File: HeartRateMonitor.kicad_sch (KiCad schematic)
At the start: 18 parts, among them J1 USB_C_Receptacle_USB2.0, U1 CH340E, U2 STM32G071KxT

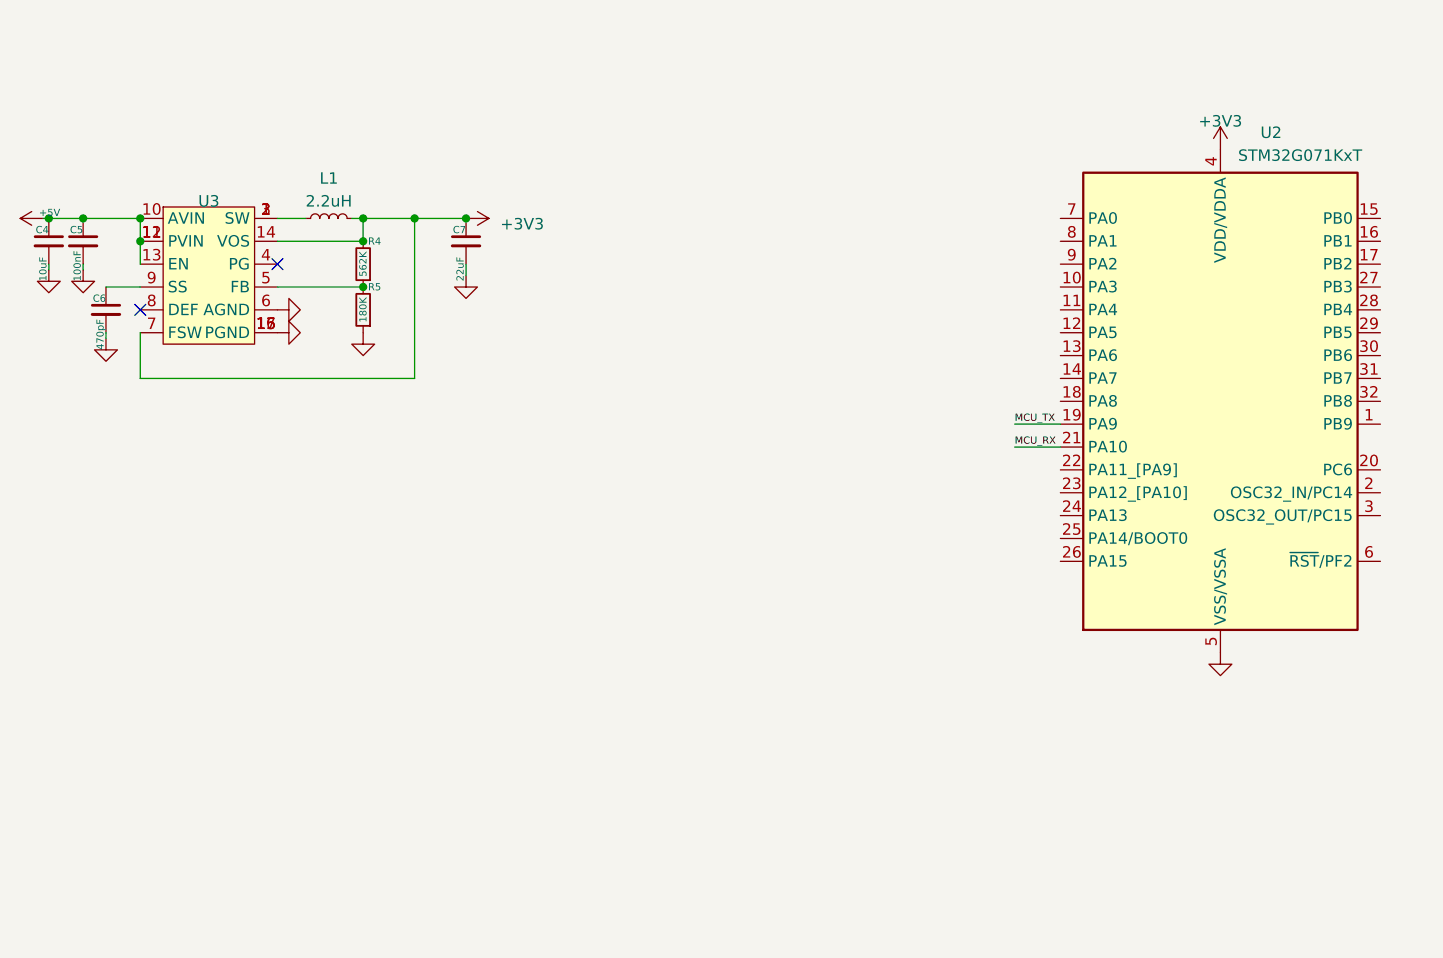
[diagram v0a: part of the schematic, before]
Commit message: firmware template and PCB constrains
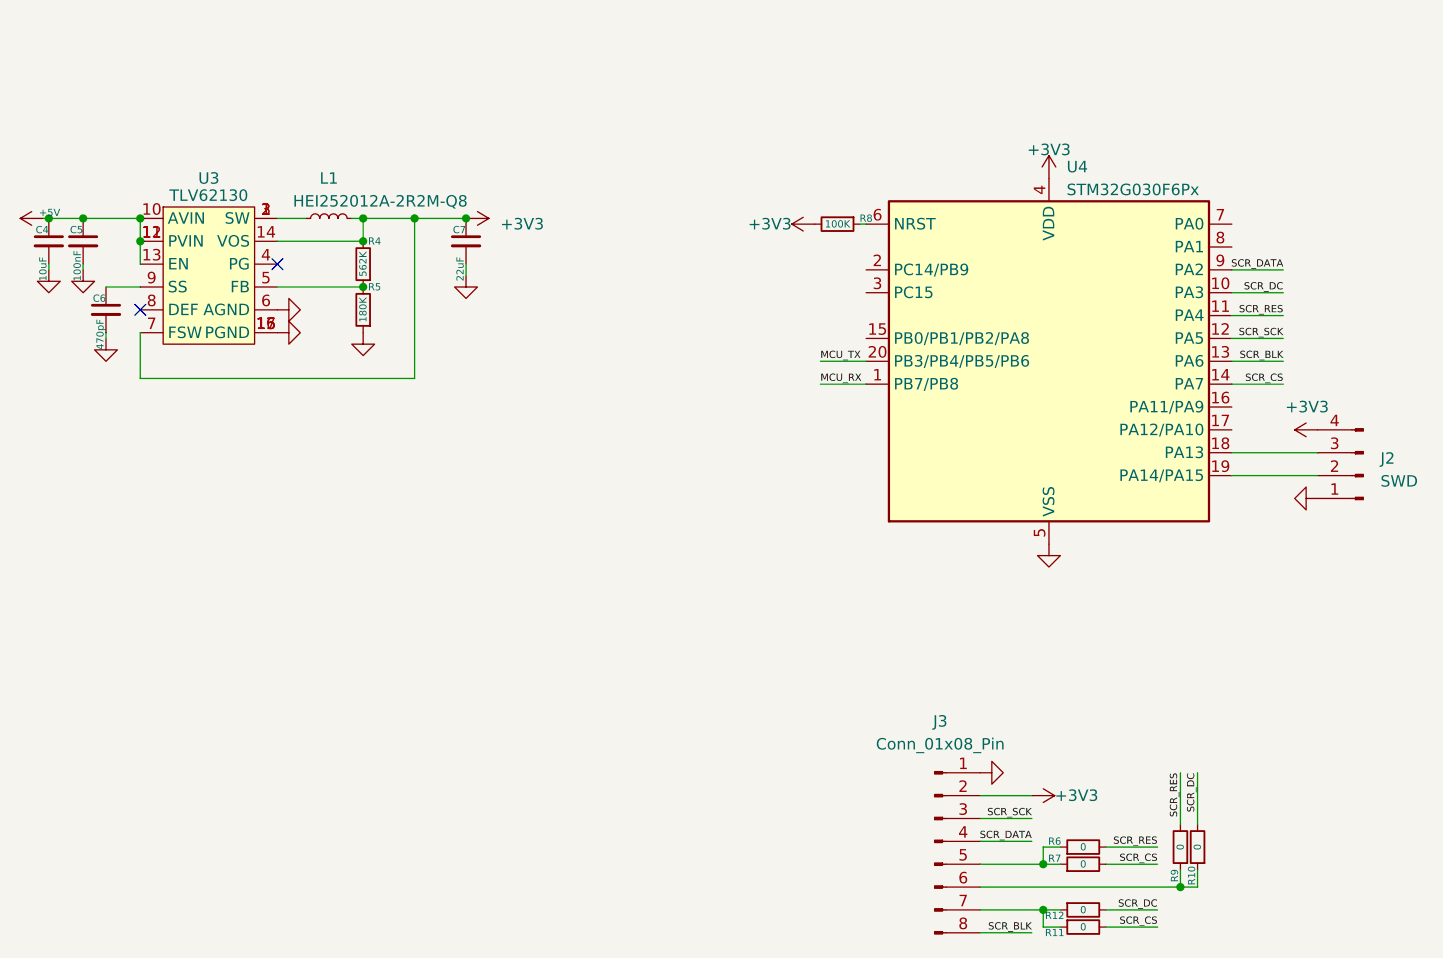
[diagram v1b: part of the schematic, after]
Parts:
- removed U2: STM32G071KxT, Package_QFP:LQFP-32_7x7mm_P0.8mm, symbol MCU_ST_STM32G0:STM32G071KxT
- added J2: SWD, Connector_PinHeader_2.54mm:PinHeader_1x04_P2.54mm_Vertical, symbol Connector:Conn_01x04_Pin
- added J3: Conn_01x08_Pin, Connector_PinHeader_2.54mm:PinHeader_1x08_P2.54mm_Vertical, symbol Connector:Conn_01x08_Pin
- added R10, R11, R12, R6, R7, R9: 0, Resistor_SMD:R_0603_1608Metric, symbol Device:R_Small
- added R8: 100K, Resistor_SMD:R_0603_1608Metric, symbol Device:R_Small
- added U4: STM32G030F6Px, Package_SO:TSSOP-20_4.4x6.5mm_P0.65mm, symbol MCU_ST_STM32G0:STM32G030F6Px
- C1, C2, C3, C4, C5, C6, C7: footprint (none) -> Capacitor_SMD:C_0603_1608Metric
- F1: footprint (none) -> Fuse:Fuse_0805_2012Metric
- J1: footprint (none) -> FP:TYPE-C-31-M-31
- L1: value 2.2uH -> HEI252012A-2R2M-Q8; footprint (none) -> Inductor_SMD:L_1008_2520Metric
- R1, R2, R3, R4, R5: footprint (none) -> Resistor_SMD:R_0603_1608Metric
- U3: value ~ -> TLV62130; footprint (none) -> Package_DFN_QFN:VQFN-16-1EP_3x3mm_P0.5mm_EP1.68x1.68mm
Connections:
- net +3V3: now also J2.4 (Pin_4), J3.2 (Pin_2), R8.2, U4.4 (VDD)
- net GND: now also J2.1 (Pin_1), J3.1 (Pin_1), U4.5 (VSS)
- net MCU_RX: now also U4.1 (PB7/PB8)
- net MCU_TX: now also U4.20 (PB3/PB4/PB5/PB6)
- new net: J3.7 (Pin_7), R11.1, R12.1
- new net: J3.5 (Pin_5), R6.1, R7.1
- new net: J2.2 (Pin_2), U4.19 (PA14/PA15)
- new net: J2.3 (Pin_3), U4.18 (PA13)
- new net: R8.1, U4.6 (NRST)
- new net: J3.6 (Pin_6), R10.1, R9.1
- new net SCR_BLK: J3.8 (Pin_8), U4.13 (PA6)
- new net SCR_CS: R11.2, R7.2, U4.14 (PA7)
- new net SCR_DATA: J3.4 (Pin_4), U4.9 (PA2)
- new net SCR_DC: R10.2, R12.2, U4.10 (PA3)
- new net SCR_RES: R6.2, R9.2, U4.11 (PA4)
- new net SCR_SCK: J3.3 (Pin_3), U4.12 (PA5)

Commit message: add TIA
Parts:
- added C8: 150pF, Capacitor_SMD:C_0603_1608Metric, symbol Device:C_Small
- added R13: 500K, Resistor_SMD:R_0603_1608Metric, symbol Device:R_Small
- added U2: LMH6702MF, Package_TO_SOT_SMD:SOT-23-5, symbol Amplifier_Operational:LMH6702MF
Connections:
- net +3V3: now also U2.5 (V+)
- net GND: now also U2.3 (+)
- new net: C8.1, R13.1, U2.4 (-)
- new net: C8.2, R13.2, U2.1
- new net -3V3: U2.2 (V-)
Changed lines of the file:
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@@
   (junction (at 139.7 37.465) (diameter 0) (color 0 0 0 0)
   )
+  (junction (at 72.39 99.06) (diameter 0) (color 0 0 0 0)
+  )
   (junction (at 114.935 40.005) (diameter 0) (color 0 0 0 0)
   )
   (junction (at 215.265 109.22) (diameter 0) (color 0 0 0 0)
   )
+  (junction (at 87.63 96.52) (diameter 0) (color 0 0 0 0)
+  )
+  (junction (at 72.39 110.49) (diameter 0) (color 0 0 0 0)
+  )
   (junction (at 51.435 31.115) (diameter 0) (color 0 0 0 0)
   )
@@
   )
   (junction (at 230.505 111.76) (diameter 0) (color 0 0 0 0)
+  )
+  (junction (at 66.04 99.06) (diameter 0) (color 0 0 0 0)
   )
   (junction (at 114.935 37.465) (diameter 0) (color 0 0 0 0)
@@
     (stroke (width 0) (type default))
   )
+  (wire (pts (xy 72.39 99.06) (xy 72.39 102.87))
+    (stroke (width 0) (type default))
+  )
   (wire (pts (xy 114.935 55.245) (xy 145.415 55.245))
     (stroke (width 0) (type default))
@@
     (stroke (width 0) (type default))
   )
+  (wire (pts (xy 72.39 110.49) (xy 66.04 110.49))
+    (stroke (width 0) (type default))
+  )
   (wire (pts (xy 145.415 55.245) (xy 145.415 37.465))
     (stroke (width 0) (type default))
@@
     (stroke (width 0) (type default))
   )
+  (wire (pts (xy 67.31 99.06) (xy 66.04 99.06))
+    (stroke (width 0) (type default))
+  )
   (wire (pts (xy 21.59 62.865) (xy 23.495 62.865))
     (stroke (width 0) (type default))
@@
     (stroke (width 0) (type default))
   )
+  (wire (pts (xy 87.63 96.52) (xy 92.71 96.52))
+    (stroke (width 0) (type default))
+  )
   (wire (pts (xy 208.28 111.76) (xy 230.505 111.76))
     (stroke (width 0) (type default))
@@
     (stroke (width 0) (type default))
   )
+  (wire (pts (xy 72.39 87.63) (xy 72.39 93.98))
+    (stroke (width 0) (type default))
+  )
+  (wire (pts (xy 72.39 107.95) (xy 72.39 110.49))
+    (stroke (width 0) (type default))
+  )
   (wire (pts (xy 67.31 55.245) (xy 67.31 56.515))
     (stroke (width 0) (type default))
@@
     (stroke (width 0) (type default))
   )
+  (wire (pts (xy 87.63 96.52) (xy 87.63 110.49))
+    (stroke (width 0) (type default))
+  )
   (wire (pts (xy 23.495 67.945) (xy 25.4 67.945))
     (stroke (width 0) (type default))
   )
+  (wire (pts (xy 87.63 110.49) (xy 72.39 110.49))
+    (stroke (width 0) (type default))
+  )
   (wire (pts (xy 139.7 37.465) (xy 138.43 37.465))
     (stroke (width 0) (type default))
@@
     (stroke (width 0) (type default))
   )
+  (wire (pts (xy 66.04 99.06) (xy 66.04 110.49))
+    (stroke (width 0) (type default))
+  )
   (wire (pts (xy 108.585 37.465) (xy 114.935 37.465))
     (stroke (width 0) (type default))
@@
   )
   (wire (pts (xy 51.435 29.845) (xy 51.435 31.115))
+    (stroke (width 0) (type default))
+  )
+  (wire (pts (xy 58.42 99.06) (xy 66.04 99.06))
     (stroke (width 0) (type default))
   )
@@
     )
   )
+  (symbol (lib_id "power:+3V3") (at 77.47 88.9 0) (unit 1)
+    (in_bom yes) (on_board yes) (dnp no) (fields_autoplaced)
+    (property "Reference" "#PWR025" (at 77.47 92.71 0)
+      (effects (font (size 1.27 1.27)) hide)
+    )
+    (property "Value" "+3V3" (at 77.47 85.09 0)
+      (effects (font (size 1.27 1.27)))
+    )
+    (property "Footprint" "" (at 77.47 88.9 0)
+      (effects (font (size 1.27 1.27)) hide)
+    )
+    (property "Datasheet" "" (at 77.47 88.9 0)
+      (effects (font (size 1.27 1.27)) hide)
+    )
+    (pin "1")
+    (instances
+      (project "HeartRateMonitor"
+        (path "/3e6a4c48-106f-4ca3-959b-b6cbb3b5c31c"
+          (reference "#PWR025") (unit 1)
+        )
+      )
+    )
+  )
   (symbol (lib_id "Device:L_Small") (at 135.89 37.465 90) (unit 1)
     (in_bom yes) (on_board yes) (dnp no)
@@
     )
   )
+  (symbol (lib_id "power:-3V3") (at 77.47 104.14 180) (unit 1)
+    (in_bom yes) (on_board yes) (dnp no) (fields_autoplaced)
+    (property "Reference" "#PWR026" (at 77.47 106.68 0)
+      (effects (font (size 1.27 1.27)) hide)
+    )
+    (property "Value" "-3V3" (at 77.47 109.22 0)
+      (effects (font (size 1.27 1.27)))
+    )
+    (property "Footprint" "" (at 77.47 104.14 0)
+      (effects (font (size 1.27 1.27)) hide)
+    )
+    (property "Datasheet" "" (at 77.47 104.14 0)
+      (effects (font (size 1.27 1.27)) hide)
+    )
+    (pin "1")
+    (instances
+      (project "HeartRateMonitor"
+        (path "/3e6a4c48-106f-4ca3-959b-b6cbb3b5c31c"
+          (reference "#PWR026") (unit 1)
+        )
+      )
+    )
+  )
   (symbol (lib_id "Device:R_Small") (at 192.405 38.1 270) (unit 1)
     (in_bom yes) (on_board yes) (dnp no)
@@
         (path "/3e6a4c48-106f-4ca3-959b-b6cbb3b5c31c"
           (reference "R8") (unit 1)
+        )
+      )
+    )
+  )
+  (symbol (lib_id "Device:C_Small") (at 69.85 99.06 270) (mirror x) (unit 1)
+    (in_bom yes) (on_board yes) (dnp no)
+    (property "Reference" "C8" (at 71.12 99.06 0)
+      (effects (font (size 0.8 0.8)) (justify left))
+    )
+    (property "Value" "150pF" (at 64.77 97.79 90)
+      (effects (font (size 0.8 0.8)) (justify left))
+    )
+    (property "Footprint" "Capacitor_SMD:C_0603_1608Metric" (at 69.85 99.06 0)
+      (effects (font (size 1.27 1.27)) hide)
+    )
+    (property "Datasheet" "~" (at 69.85 99.06 0)
+      (effects (font (size 1.27 1.27)) hide)
+    )
+    (pin "1")
+    (pin "2")
+    (instances
+      (project "HeartRateMonitor"
+        (path "/3e6a4c48-106f-4ca3-959b-b6cbb3b5c31c"
+          (reference "C8") (unit 1)
         )
       )
@@
     )
   )
+  (symbol (lib_id "power:GND") (at 72.39 87.63 180) (unit 1)
+    (in_bom yes) (on_board yes) (dnp no) (fields_autoplaced)
+    (property "Reference" "#PWR027" (at 72.39 81.28 0)
+      (effects (font (size 1.27 1.27)) hide)
+    )
+    (property "Value" "GND" (at 72.39 83.185 0)
+      (effects (font (size 1.27 1.27)) hide)
+    )
+    (property "Footprint" "" (at 72.39 87.63 0)
+      (effects (font (size 1.27 1.27)) hide)
+    )
+    (property "Datasheet" "" (at 72.39 87.63 0)
+      (effects (font (size 1.27 1.27)) hide)
+    )
+    (pin "1")
+    (instances
+      (project "HeartRateMonitor"
+        (path "/3e6a4c48-106f-4ca3-959b-b6cbb3b5c31c"
+          (reference "#PWR027") (unit 1)
+        )
+      )
+    )
+  )
   (symbol (lib_id "Device:R_Small") (at 219.71 107.315 90) (unit 1)
     (in_bom yes) (on_board yes) (dnp no)
@@
     )
   )
+  (symbol (lib_id "Amplifier_Operational:LMH6702MF") (at 80.01 96.52 0) (unit 1)
+    (in_bom yes) (on_board yes) (dnp no)
+    (property "Reference" "U2" (at 86.36 88.9 0)
+      (effects (font (size 1.27 1.27)))
+    )
+    (property "Value" "LMH6702MF" (at 86.36 91.44 0)
+      (effects (font (size 1.27 1.27)))
+    )
+    (property "Footprint" "Package_TO_SOT_SMD:SOT-23-5" (at 77.47 101.6 0)
+      (effects (font (size 1.27 1.27)) (justify left) hide)
+    )
+    (property "Datasheet" "http://www.ti.com/lit/ds/symlink/lmh6702.pdf" (at 80.01 91.44 0)
+      (effects (font (size 1.27 1.27)) hide)
+    )
+    (pin "2")
+    (pin "5")
+    (pin "1")
+    (pin "3")
+    (pin "4")
+    (instances
+      (project "HeartRateMonitor"
+        (path "/3e6a4c48-106f-4ca3-959b-b6cbb3b5c31c"
+          (reference "U2") (unit 1)
+        )
+      )
+    )
+  )
   (symbol (lib_id "power:GND") (at 108.585 43.18 0) (unit 1)
     (in_bom yes) (on_board yes) (dnp no) (fields_autoplaced)
@@
         )
       )
+    )
+  )
+  (symbol (lib_id "Device:R_Small") (at 72.39 105.41 0) (unit 1)
+    (in_bom yes) (on_board yes) (dnp no)
+    (property "Reference" "R13" (at 71.12 105.41 90)
+      (effects (font (size 0.8 0.8)))
+    )
+    (property "Value" "500K" (at 72.39 105.41 90)
+      (effects (font (size 0.8 0.8)))
+    )
+    (property "Footprint" "Resistor_SMD:R_0603_1608Metric" (at 72.39 105.41 0)
+      (effects (font (size 1.27 1.27)) hide)
+    )
+    (property "Datasheet" "~" (at 72.39 105.41 0)
+      (effects (font (size 1.27 1.27)) hide)
+    )
+    (pin "1")
+    (pin "2")
+    (instances
+      (project "HeartRateMonitor"
+        (path "/3e6a4c48-106f-4ca3-959b-b6cbb3b5c31c"
+          (reference "R13") (unit 1)
+        )
+      )
